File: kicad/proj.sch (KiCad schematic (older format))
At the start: 22 parts, among them J1 XLR, J2 XLR, J3 CONN_PWR, J4 CONN_S1A, J5 CONN_S1B, U1 INA217, U2 NE5532

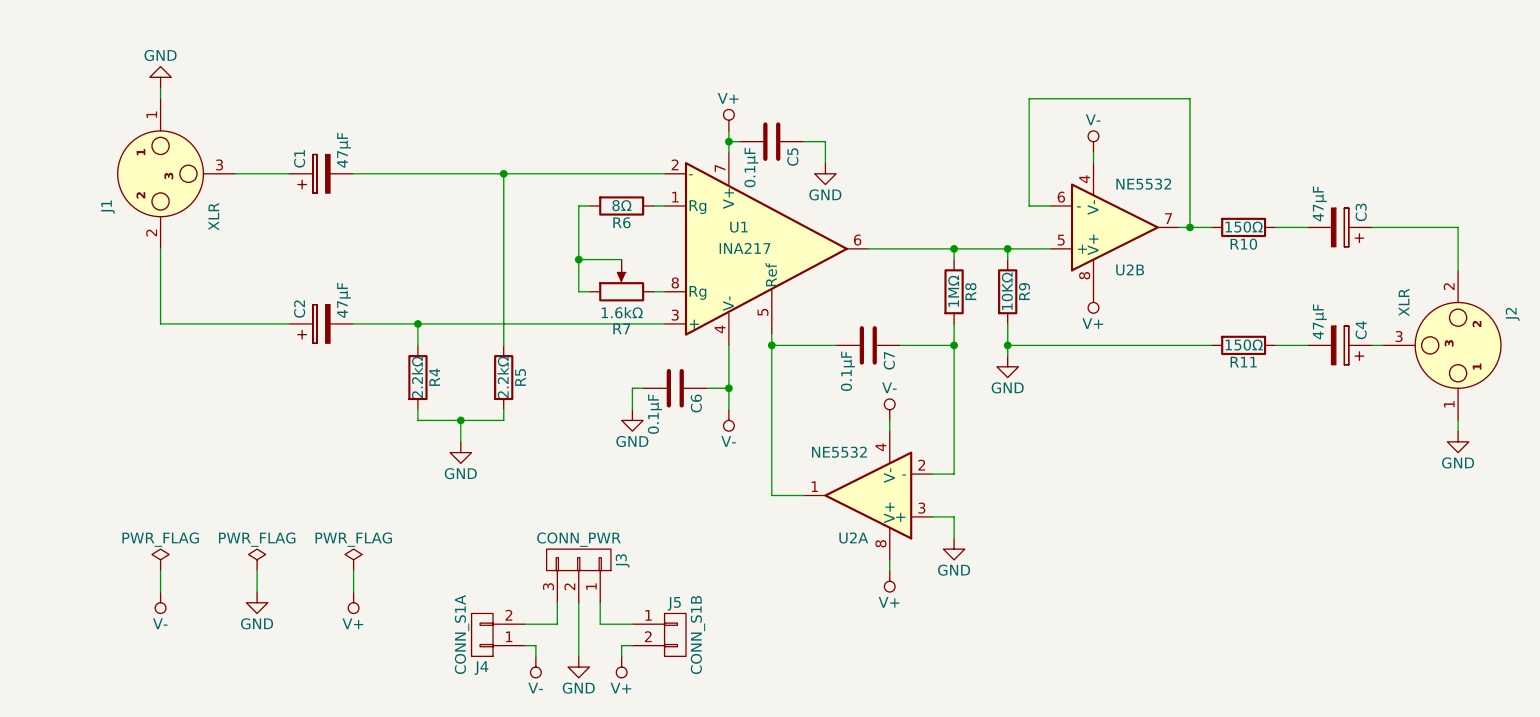
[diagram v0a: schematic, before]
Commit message: Change C1-4 to non-polar and connected XLR pin 1s to chassis, only GND at input
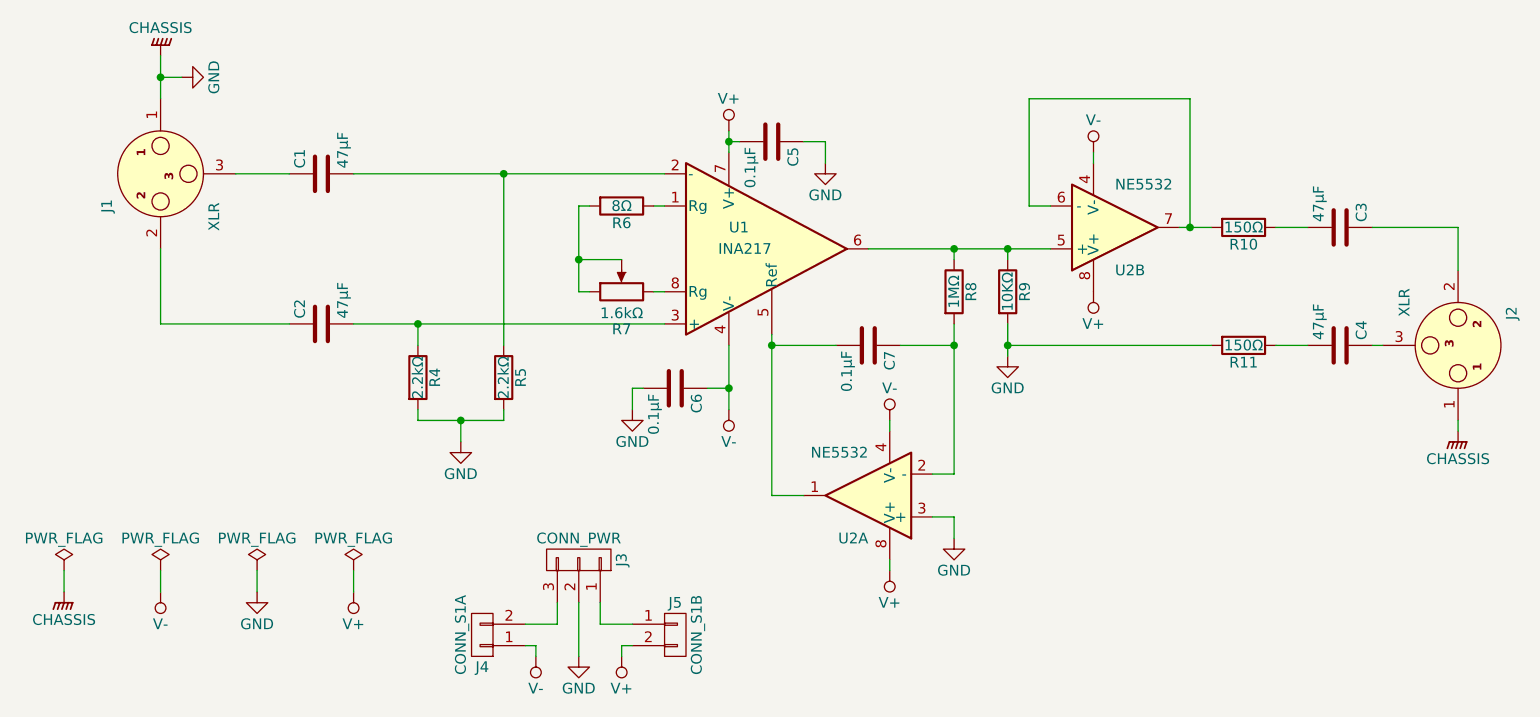
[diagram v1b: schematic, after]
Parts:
- removed C1, C2, C3, C4: 47μF, Capacitors_THT:CP_Radial_D10.0mm_P5.00mm, symbol CP
- added C1, C2, C3, C4: 47μF, Capacitors_THT:CP_Radial_D10.0mm_P5.00mm, symbol C
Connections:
- net at J1.2: now also C2.1
- net at J1.3: now also C1.1
- net at R5.1, U1.2 (-): now also C1.2
- net at R4.1, U1.3 (+): now also C2.2
- net at J2.2: now also C3.1
- net at J2.3: now also C4.1
- net at R10.1: now also C3.2
- net at R11.1: now also C4.2
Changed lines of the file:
@@
 LIBS:v-
 LIBS:v+
+LIBS:chassis
 LIBS:proj-cache
 EELAYER 25 0
@@
 $EndComp
 $Comp
-L GND #PWR03
-U 1 1 5928971A
-P 8550 4350
-F 0 "#PWR03" H 8550 4100 50  0001 C CNN
-F 1 "GND" H 8550 4200 50  0000 C CNN
-F 2 "" H 8550 4350 50  0001 C CNN
-F 3 "" H 8550 4350 50  0001 C CNN
-	1    8550 4350
-	1    0    0    -1
-$EndComp
-$Comp
 L R R8
 U 1 1 5928C3AB
@@
 $EndComp
 $Comp
-L GND #PWR04
+L GND #PWR03
 U 1 1 592B10C6
 P 6450 4000
-F 0 "#PWR04" H 6450 3750 50  0001 C CNN
+F 0 "#PWR03" H 6450 3750 50  0001 C CNN
 F 1 "GND" H 6450 3850 50  0000 C CNN
 F 2 "" H 6450 4000 50  0001 C CNN
@@
 $EndComp
 $Comp
+L GND #PWR04
+U 1 1 592B4DDB
+P 2600 2700
+F 0 "#PWR04" H 2600 2450 50  0001 C CNN
+F 1 "GND" H 2600 2550 50  0000 C CNN
+F 2 "" H 2600 2700 50  0001 C CNN
+F 3 "" H 2600 2700 50  0001 C CNN
+	1    2600 2700
+	0    -1   1    0
+$EndComp
+$Comp
 L GND #PWR05
-U 1 1 592B4DDB
-P 2500 2750
-F 0 "#PWR05" H 2500 2500 50  0001 C CNN
-F 1 "GND" H 2500 2600 50  0000 C CNN
-F 2 "" H 2500 2750 50  0001 C CNN
-F 3 "" H 2500 2750 50  0001 C CNN
-	1    2500 2750
-	1    0    0    1
-$EndComp
-$Comp
-L GND #PWR06
 U 1 1 592B55B4
 P 4700 4250
-F 0 "#PWR06" H 4700 4000 50  0001 C CNN
+F 0 "#PWR05" H 4700 4000 50  0001 C CNN
 F 1 "GND" H 4700 4100 50  0000 C CNN
 F 2 "" H 4700 4250 50  0001 C CNN
@@
 $EndComp
 $Comp
-L GND #PWR07
+L GND #PWR06
 U 1 1 592B56A4
 P 6200 4850
-F 0 "#PWR07" H 6200 4600 50  0001 C CNN
+F 0 "#PWR06" H 6200 4600 50  0001 C CNN
 F 1 "GND" H 6200 4700 50  0000 C CNN
 F 2 "" H 6200 4850 50  0001 C CNN
@@
 $EndComp
 $Comp
-L PWR_FLAG #FLG08
+L PWR_FLAG #FLG07
 U 1 1 592AF6A5
 P 2500 5000
-F 0 "#FLG08" H 2500 5075 50  0001 C CNN
+F 0 "#FLG07" H 2500 5075 50  0001 C CNN
 F 1 "PWR_FLAG" H 2500 5150 50  0000 C CNN
 F 2 "" H 2500 5000 50  0001 C CNN
@@
 $EndComp
 $Comp
-L PWR_FLAG #FLG09
+L PWR_FLAG #FLG08
 U 1 1 592AF6E9
 P 2950 5000
-F 0 "#FLG09" H 2950 5075 50  0001 C CNN
+F 0 "#FLG08" H 2950 5075 50  0001 C CNN
 F 1 "PWR_FLAG" H 2950 5150 50  0000 C CNN
 F 2 "" H 2950 5000 50  0001 C CNN
@@
 $EndComp
 $Comp
-L PWR_FLAG #FLG010
+L PWR_FLAG #FLG09
 U 1 1 592AF7D5
 P 3400 5000
-F 0 "#FLG010" H 3400 5075 50  0001 C CNN
+F 0 "#FLG09" H 3400 5075 50  0001 C CNN
 F 1 "PWR_FLAG" H 3400 5150 50  0000 C CNN
 F 2 "" H 3400 5000 50  0001 C CNN
@@
 $EndComp
 $Comp
-L GND #PWR011
+L GND #PWR010
 U 1 1 592AF82F
 P 2950 5100
-F 0 "#PWR011" H 2950 4850 50  0001 C CNN
+F 0 "#PWR010" H 2950 4850 50  0001 C CNN
 F 1 "GND" H 2950 4950 50  0000 C CNN
 F 2 "" H 2950 5100 50  0001 C CNN
@@
 	1    2950 5100
 	1    0    0    -1
-$EndComp
-$Comp
-L CP C1
-U 1 1 592B05C1
-P 3250 3150
-F 0 "C1" H 3275 3250 50  0000 L CNN
-F 1 "47μF" H 3275 3050 50  0000 L CNN
-F 2 "Capacitors_THT:CP_Radial_D10.0mm_P5.00mm" H 3288 3000 50  0001 C CNN
-F 3 "" H 3250 3150 50  0001 C CNN
-	1    3250 3150
-	0    -1   -1   0
-$EndComp
-$Comp
-L CP C2
-U 1 1 592B0BCB
-P 3250 3850
-F 0 "C2" H 3275 3950 50  0000 L CNN
-F 1 "47μF" H 3275 3750 50  0000 L CNN
-F 2 "Capacitors_THT:CP_Radial_D10.0mm_P5.00mm" H 3288 3700 50  0001 C CNN
-F 3 "" H 3250 3850 50  0001 C CNN
-	1    3250 3850
-	0    -1   -1   0
-$EndComp
-$Comp
-L CP C3
-U 1 1 592B0C8A
-P 8000 3400
-F 0 "C3" H 8025 3500 50  0000 L CNN
-F 1 "47μF" H 8025 3300 50  0000 L CNN
-F 2 "Capacitors_THT:CP_Radial_D10.0mm_P5.00mm" H 8038 3250 50  0001 C CNN
-F 3 "" H 8000 3400 50  0001 C CNN
-	1    8000 3400
-	0    1    -1   0
-$EndComp
-$Comp
-L CP C4
-U 1 1 592B0D19
-P 8000 3950
-F 0 "C4" H 8025 4050 50  0000 L CNN
-F 1 "47μF" H 8025 3850 50  0000 L CNN
-F 2 "Capacitors_THT:CP_Radial_D10.0mm_P5.00mm" H 8038 3800 50  0001 C CNN
-F 3 "" H 8000 3950 50  0001 C CNN
-	1    8000 3950
-	0    1    -1   0
 $EndComp
 $Comp
@@
 	2850 3150 3100 3150
 Wire Wire Line
-	2500 2750 2500 2800
-Wire Wire Line
 	2500 3500 2500 3850
 Wire Wire Line
@@
 	4450 5150 4450 5400
 $Comp
-L GND #PWR012
+L GND #PWR011
 U 1 1 592B4D1B
 P 4450 5400
-F 0 "#PWR012" H 4450 5150 50  0001 C CNN
+F 0 "#PWR011" H 4450 5150 50  0001 C CNN
 F 1 "GND" H 4450 5250 50  0000 C CNN
 F 2 "" H 4450 5400 50  0001 C CNN
@@
 	4250 5350 4250 5400
 $Comp
-L V+ #PWR013
+L V+ #PWR012
 U 1 1 592E5B2E
 P 5150 2950
-F 0 "#PWR013" H 5150 2800 50  0001 C CNN
+F 0 "#PWR012" H 5150 2800 50  0001 C CNN
 F 1 "V+" H 5150 3100 50  0000 C CNN
 F 2 "" H 5150 2950 50  0001 C CNN
@@
 $EndComp
 $Comp
-L V- #PWR014
+L V- #PWR013
 U 1 1 592E5B70
 P 6850 3050
-F 0 "#PWR014" H 6850 2900 50  0001 C CNN
+F 0 "#PWR013" H 6850 2900 50  0001 C CNN
 F 1 "V-" H 6850 3200 50  0000 C CNN
 F 2 "" H 6850 3050 50  0001 C CNN
@@
 $EndComp
 $Comp
-L V- #PWR015
+L V- #PWR014
 U 1 1 592E5C16
 P 5150 4250
-F 0 "#PWR015" H 5150 4100 50  0001 C CNN
+F 0 "#PWR014" H 5150 4100 50  0001 C CNN
 F 1 "V-" H 5150 4400 50  0000 C CNN
 F 2 "" H 5150 4250 50  0001 C CNN
@@
 $EndComp
 $Comp
-L V- #PWR016
+L V- #PWR015
 U 1 1 592E5C66
 P 5900 4300
-F 0 "#PWR016" H 5900 4150 50  0001 C CNN
+F 0 "#PWR015" H 5900 4150 50  0001 C CNN
 F 1 "V-" H 5900 4450 50  0000 C CNN
 F 2 "" H 5900 4300 50  0001 C CNN
@@
 $EndComp
 $Comp
-L V+ #PWR017
+L V+ #PWR016
 U 1 1 592E5D05
 P 5900 5000
-F 0 "#PWR017" H 5900 4850 50  0001 C CNN
+F 0 "#PWR016" H 5900 4850 50  0001 C CNN
 F 1 "V+" H 5900 5150 50  0000 C CNN
 F 2 "" H 5900 5000 50  0001 C CNN
@@
 $EndComp
 $Comp
-L V+ #PWR018
+L V+ #PWR017
 U 1 1 592E5DB2
 P 6850 3700
-F 0 "#PWR018" H 6850 3550 50  0001 C CNN
+F 0 "#PWR017" H 6850 3550 50  0001 C CNN
 F 1 "V+" H 6850 3850 50  0000 C CNN
 F 2 "" H 6850 3700 50  0001 C CNN
@@
 $EndComp
 $Comp
-L V- #PWR019
+L V- #PWR018
 U 1 1 592E5E75
 P 2500 5100
-F 0 "#PWR019" H 2500 4950 50  0001 C CNN
+F 0 "#PWR018" H 2500 4950 50  0001 C CNN
 F 1 "V-" H 2500 5250 50  0000 C CNN
 F 2 "" H 2500 5100 50  0001 C CNN
@@
 $EndComp
 $Comp
-L V- #PWR020
+L V- #PWR019
 U 1 1 592E5EC5
 P 4250 5400
-F 0 "#PWR020" H 4250 5250 50  0001 C CNN
+F 0 "#PWR019" H 4250 5250 50  0001 C CNN
 F 1 "V-" H 4250 5550 50  0000 C CNN
 F 2 "" H 4250 5400 50  0001 C CNN
@@
 $EndComp
 $Comp
-L V+ #PWR021
+L V+ #PWR020
 U 1 1 592E5FB6
 P 3400 5100
-F 0 "#PWR021" H 3400 4950 50  0001 C CNN
+F 0 "#PWR020" H 3400 4950 50  0001 C CNN
 F 1 "V+" H 3400 5250 50  0000 C CNN
 F 2 "" H 3400 5100 50  0001 C CNN
@@
 $EndComp
 $Comp
-L V+ #PWR022
+L V+ #PWR021
 U 1 1 592E6006
 P 4650 5400
-F 0 "#PWR022" H 4650 5250 50  0001 C CNN
+F 0 "#PWR021" H 4650 5250 50  0001 C CNN
 F 1 "V+" H 4650 5550 50  0000 C CNN
 F 2 "" H 4650 5400 50  0001 C CNN
@@
 Wire Wire Line
 	7700 3950 7850 3950
+Wire Wire Line
+	2500 2600 2500 2800
+Wire Wire Line
+	2600 2700 2500 2700
+Connection ~ 2500 2700
+$Comp
+L PWR_FLAG #FLG022
+U 1 1 5954452E
+P 2050 5000
+F 0 "#FLG022" H 2050 5075 50  0001 C CNN
+F 1 "PWR_FLAG" H 2050 5150 50  0000 C CNN
+F 2 "" H 2050 5000 50  0001 C CNN
+F 3 "" H 2050 5000 50  0001 C CNN
+	1    2050 5000
+	1    0    0    -1
+$EndComp
+Wire Wire Line
+	2050 5000 2050 5100
+$Comp
+L CHASSIS #PWR023
+U 1 1 59544734
+P 2050 5100
+F 0 "#PWR023" H 2050 4900 50  0001 C CNN
+F 1 "CHASSIS" H 2050 4970 50  0000 C CNN
+F 2 "" H 2050 5050 50  0001 C CNN
+F 3 "" H 2050 5050 50  0001 C CNN
+	1    2050 5100
+	1    0    0    -1
+$EndComp
+$Comp
+L CHASSIS #PWR024
+U 1 1 595447BA
+P 2500 2600
+F 0 "#PWR024" H 2500 2400 50  0001 C CNN
+F 1 "CHASSIS" H 2500 2470 50  0000 C CNN
+F 2 "" H 2500 2550 50  0001 C CNN
+F 3 "" H 2500 2550 50  0001 C CNN
+	1    2500 2600
+	-1   0    0    1
+$EndComp
+$Comp
+L CHASSIS #PWR025
+U 1 1 59544C71
+P 8550 4350
+F 0 "#PWR025" H 8550 4150 50  0001 C CNN
+F 1 "CHASSIS" H 8550 4220 50  0000 C CNN
+F 2 "" H 8550 4300 50  0001 C CNN
+F 3 "" H 8550 4300 50  0001 C CNN
+	1    8550 4350
+	1    0    0    -1
+$EndComp
+$Comp
+L C C1
+U 1 1 59544F46
+P 3250 3150
+F 0 "C1" H 3275 3250 50  0000 L CNN
+F 1 "47μF" H 3275 3050 50  0000 L CNN
+F 2 "Capacitors_THT:CP_Radial_D10.0mm_P5.00mm" H 3288 3000 50  0001 C CNN
+F 3 "" H 3250 3150 50  0001 C CNN
+	1    3250 3150
+	0    -1   -1   0
+$EndComp
+$Comp
+L C C2
+U 1 1 59545297
+P 3250 3850
+F 0 "C2" H 3275 3950 50  0000 L CNN
+F 1 "47μF" H 3275 3750 50  0000 L CNN
+F 2 "Capacitors_THT:CP_Radial_D10.0mm_P5.00mm" H 3288 3700 50  0001 C CNN
+F 3 "" H 3250 3850 50  0001 C CNN
+	1    3250 3850
+	0    -1   -1   0
+$EndComp
+$Comp
+L C C3
+U 1 1 595453AE
+P 8000 3400
+F 0 "C3" H 8025 3500 50  0000 L CNN
+F 1 "47μF" H 8025 3300 50  0000 L CNN
+F 2 "Capacitors_THT:CP_Radial_D10.0mm_P5.00mm" H 8038 3250 50  0001 C CNN
+F 3 "" H 8000 3400 50  0001 C CNN
+	1    8000 3400
+	0    1    -1   0
+$EndComp
+$Comp
+L C C4
+U 1 1 59545546
+P 8000 3950
+F 0 "C4" H 8025 4050 50  0000 L CNN
+F 1 "47μF" H 8025 3850 50  0000 L CNN
+F 2 "Capacitors_THT:CP_Radial_D10.0mm_P5.00mm" H 8038 3800 50  0001 C CNN
+F 3 "" H 8000 3950 50  0001 C CNN
+	1    8000 3950
+	0    1    -1   0
+$EndComp
 $EndSCHEMATC
